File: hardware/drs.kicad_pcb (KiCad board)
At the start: 4 copper layers, 60 x 40 mm, 100 parts, among them IC1 TPS54202HDDCR, J1 USB-C_GCT_USB4145-03-0070-C, J2 FTSH-107-01-L-D-K, J3 POWER & CAN & SPI2, J4 PWM1, J5 PWM2, Q1 SI2347DS-T1-GE3, Q2 LMR51635XDDCR, Q3 LMR51635XDDCR, T1 TP_VCC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

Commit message: signal routing
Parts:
- moved T5 42.5 mm to (207.2, 93.5)
- moved R15 2.00 mm to (162.5, 79.8)
- moved R16 1.55 mm to (162.5, 78.0)
- moved J4 0.60 mm to (174.2, 87.0)
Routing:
- net +3V3: track 3.39 -> 84.5 mm, vias 0 -> 5
- net VCC: track 6.24 -> 79.1 mm, vias 0 -> 7
- net VBUS: track 0.00 -> 49.5 mm, vias 0 -> 6
- net /Connectors/RX: track 0.00 -> 49.2 mm, vias 0 -> 3
- net +6V6S2: track 0.00 -> 48.9 mm, vias 0 -> 2
- net /Connectors/CLK: track 0.00 -> 48.4 mm, vias 0 -> 3
- net /Control/NRST: track 2.96 -> 50.5 mm, vias 0 -> 2
- net +6V6S1: track 0.00 -> 47.5 mm
- net /Connectors/PWM2: track 0.00 -> 43.2 mm, vias 0 -> 2
- net /Connectors/PWM1: track 0.00 -> 43.0 mm, vias 0 -> 1
- net /Connectors/TX: track 0.00 -> 37.3 mm, vias 0 -> 1
- net /Connectors/DIO: track 0.00 -> 36.6 mm, vias 0 -> 1
- net /Connectors/D-: track 0.00 -> 29.4 mm, vias 0 -> 2
- net /Connectors/D+: track 0.00 -> 28.5 mm, vias 0 -> 2
- net CAN_H: track 9.95 -> 38.2 mm, vias 0 -> 1
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- added copper zone on F.Cu, net /Power/+6V6S2_OUT
- added copper zone on B.Cu, net /Power/SW_+6V6S2
- added copper zone on F.Cu, net /Power/SW_+6V6S2

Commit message: usbc changed, foots for electro cap and +5 lay
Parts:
- added C14: 22u, Capacitor_SMD:CP_Elec_4x5.8, F.Cu at (239.6, 99.5)
- added C16: 22u, Capacitor_SMD:CP_Elec_4x5.8, F.Cu at (232.0, 99.5)
- C24, C30, C31: footprint Capacitor_SMD:C_0805_2012Metric -> Capacitor_SMD:C_0805_2012Metric_Pad1.18x1.45mm_HandSolder
- C25: footprint Capacitor_SMD:C_0603_1608Metric -> Capacitor_SMD:C_0603_1608Metric_Pad1.08x0.95mm_HandSolder
- C29: renamed from C28; footprint Capacitor_SMD:C_0805_2012Metric -> Capacitor_SMD:C_0805_2012Metric_Pad1.18x1.45mm_HandSolder
- F4, F5: footprint Fuse:Fuse_1812_4532Metric_Pad1.30x3.40mm_HandSolder -> Fuse:Fuse_0805_2012Metric_Pad1.15x1.40mm_HandSolder
- J1: footprint SamacSys_Parts:USB4145030230C -> Connector_USB:USB_C_Receptacle_GCT_USB4110
- Q3: footprint SamacSys_Parts:SOT95P280X110-6N -> Package_TO_SOT_SMD:SOT-23-6_Handsoldering
- R13: footprint Resistor_SMD:R_0603_1608Metric -> Resistor_SMD:R_0603_1608Metric_Pad0.98x0.95mm_HandSolder
- T11: value TP_+3V3 -> TP_+5V
- T9: value TP_+5V -> TP_+3V3
- moved T4 189.9 mm to (1.02, 1.02)
- moved C14 113.5 mm to (234.2, 88.5)
- moved C15 113.5 mm to (241.4, 88.0)
- moved C16 113.5 mm to (234.2, 93.8)
- moved C19 113.5 mm to (239.7, 88.0)
- moved D5 101.3 mm to (226.9, 109.2), turned to 180 degrees
- moved R11 100.5 mm to (228.1, 111.9)
- moved C24 100.4 mm to (230.9, 106.2)
- moved C25 100.4 mm to (230.9, 108.2)
- moved C27 100.4 mm to (233.6, 111.6)
- moved C29 100.4 mm to (236.8, 110.8)
- moved C30 100.4 mm to (236.8, 113.0)
- moved C31 100.4 mm to (236.8, 115.2)
- moved IC1 100.4 mm to (230.9, 111.4)
- moved L3 100.4 mm to (236.3, 106.4)
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- renumbered C18 to C17, C19 to C18, C17 to C19, C29 to C28
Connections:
- F2 pad 1: +6V6S1 -> /Power/+6V6S1_OUT
- F2 pad 2: /Power/+6V6S1_OUT -> +6V6S1
- T10 pad 1: GND -> /Power/+5V_OUT
- T11 pad 1: /Power/VO_+3.3V -> GND
- T9 pad 1: /Power/+5V_OUT -> /Power/VO_+3.3V
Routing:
- net VCC: track 79.1 -> 0.00 mm, vias 7 -> 0
- net +3V3: track 84.5 -> 6.19 mm, vias 5 -> 0
- net /Control/NRST: track 50.5 -> 0.00 mm, vias 2 -> 0
- net VBUS: track 49.5 -> 0.00 mm, vias 6 -> 0
- net /Connectors/RX: track 49.2 -> 0.00 mm, vias 3 -> 0
- net +6V6S2: track 48.9 -> 0.00 mm, vias 2 -> 0
- net /Connectors/CLK: track 48.4 -> 0.00 mm, vias 3 -> 0
- net +6V6S1: track 47.5 -> 0.00 mm
- net /Connectors/PWM2: track 43.2 -> 0.00 mm, vias 2 -> 0
- net /Connectors/PWM1: track 43.0 -> 0.00 mm, vias 1 -> 0
- net /Connectors/TX: track 37.3 -> 0.00 mm, vias 1 -> 0
- net /Connectors/DIO: track 36.6 -> 0.00 mm, vias 1 -> 0
- net /Connectors/D-: track 29.4 -> 0.00 mm, vias 2 -> 0
- net /Connectors/D+: track 28.5 -> 0.00 mm, vias 2 -> 0
- net CAN_H: track 38.2 -> 9.95 mm, vias 1 -> 0
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- added copper zone on F.Cu, net /Power/+5V_OUT
- added copper zone on F.Cu, net /Power/FB_+5V
- added copper zone on F.Cu, net /Power/SW_+5V

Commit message: pcb & footprint update
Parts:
- removed the C14 at (239.6, 99.5)
- removed the C16 at (232.0, 99.5)
- C14, C16: footprint SamacSys_Parts:CAPPM7343X310N -> Capacitor_SMD:CP_Elec_4x5.8
- C20, C21, C22, C23: footprint Capacitor_SMD:C_0603_1608Metric_Pad1.08x0.95mm_HandSolder -> Capacitor_SMD:C_0805_2012Metric_Pad1.18x1.45mm_HandSolder
- C3, C5: footprint Capacitor_SMD:C_0603_1608Metric_Pad1.08x0.95mm_HandSolder -> Capacitor_SMD:C_0201_0603Metric_Pad0.64x0.40mm_HandSolder
- D1, D2, D3, D7: footprint LED_SMD:LED_0603_1608Metric -> LED_SMD:LED_0603_1608Metric_Pad1.05x0.95mm_HandSolder
- D4: footprint Diode_SMD:D_SOD-323_HandSoldering -> Diode_SMD:D_SMB_Handsoldering
- D6: footprint Diode_SMD:D_SOD-123 -> Diode_SMD:D_SOD-123F
- D8: footprint Package_TO_SOT_SMD:SOT-23 -> Package_TO_SOT_SMD:SOT-23-3
- F1: footprint Fuse:Fuse_1206_3216Metric_Pad1.42x1.75mm_HandSolder -> Fuse:Fuse_0805_2012Metric_Pad1.15x1.40mm_HandSolder
- IC1: footprint Package_TO_SOT_SMD:SOT-23-6 -> Package_TO_SOT_SMD:SOT-23-6_Handsoldering
- J1: value USB-C_GCT_USB4145-03-0070-C -> USB_C_Receptacle_USB2.0_16P; footprint Connector_USB:USB_C_Receptacle_GCT_USB4110 -> Connector_USB:USB_C_Receptacle_GCT_USB4105-xx-A_16P_TopMnt_Horizontal
- Q1: footprint Package_TO_SOT_SMD:SOT-23_Handsoldering -> Package_TO_SOT_SMD:SOT-23-3
- R11, R12: footprint Resistor_SMD:R_0603_1608Metric -> Resistor_SMD:R_0603_1608Metric_Pad0.98x0.95mm_HandSolder
- moved C15 21.8 mm to (220.0, 91.8)
- moved C19 21.8 mm to (218.2, 91.8)
- moved C14 20.7 mm to (218.6, 102.0), turned to 0 degrees
- moved C16 15.2 mm to (219.2, 96.5), turned to 0 degrees
- moved C18 12.8 mm to (233.5, 88.1)
- moved C9 12.8 mm to (240.3, 94.3)
- moved L2 12.8 mm to (236.5, 82.9)
- moved Q3 12.8 mm to (236.2, 90.3)
- moved R10 12.8 mm to (235.3, 94.3)
- moved R9 12.8 mm to (233.5, 92.5)
- moved C11 12.8 mm to (238.7, 94.3)
- moved C13 12.8 mm to (237.1, 94.3)
- moved C21 12.8 mm to (241.8, 80.8)
- moved C23 12.8 mm to (241.8, 79.2)
- moved C7 12.8 mm to (239.1, 89.5)
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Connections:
- D4 pad 2: /Power/RPP_D -> /Power/RPP_G
- D5 pad 2: /Power/RPP_G -> /Power/RPP_S
- F1 pad 2: /Power/RPP_D -> /Power/RPP_G
- J1 pad A6: /Connectors/D- -> /Connectors/D+
- J1 pad B7: /Connectors/D+ -> /Connectors/D-
- J1 pad S1: (no net) -> GND
- Q1 pad 1: /Power/RPP_D -> /Power/RPP_G
- Q1 pad 2: /Power/RPP_G -> /Power/RPP_S
- R6 pad 1: /Power/RPP_G -> /Power/RPP_S
- T3 pad 1: /Power/RPP_D -> /Power/RPP_G
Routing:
- removed copper zone on In2.Cu, net (none)
- removed copper zone on In1.Cu, net GND

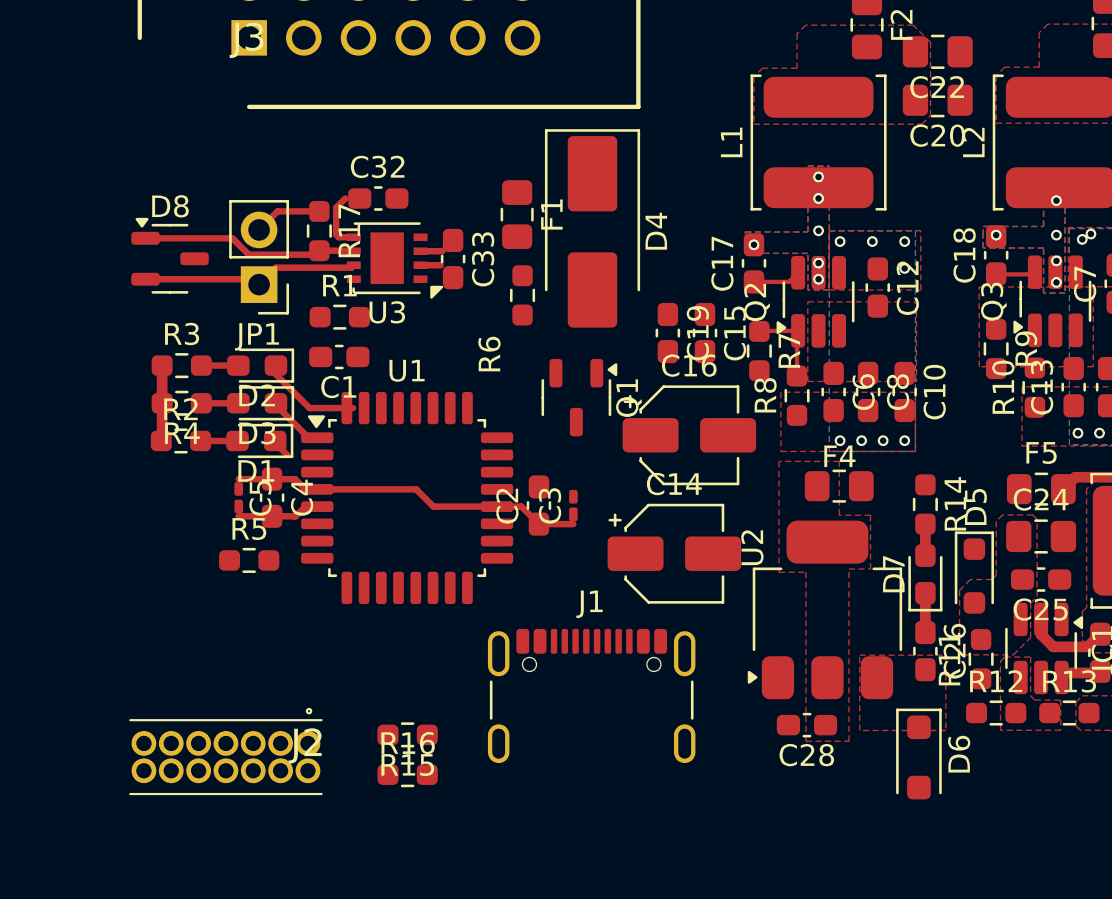
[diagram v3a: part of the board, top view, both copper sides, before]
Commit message: d4 - footprint change
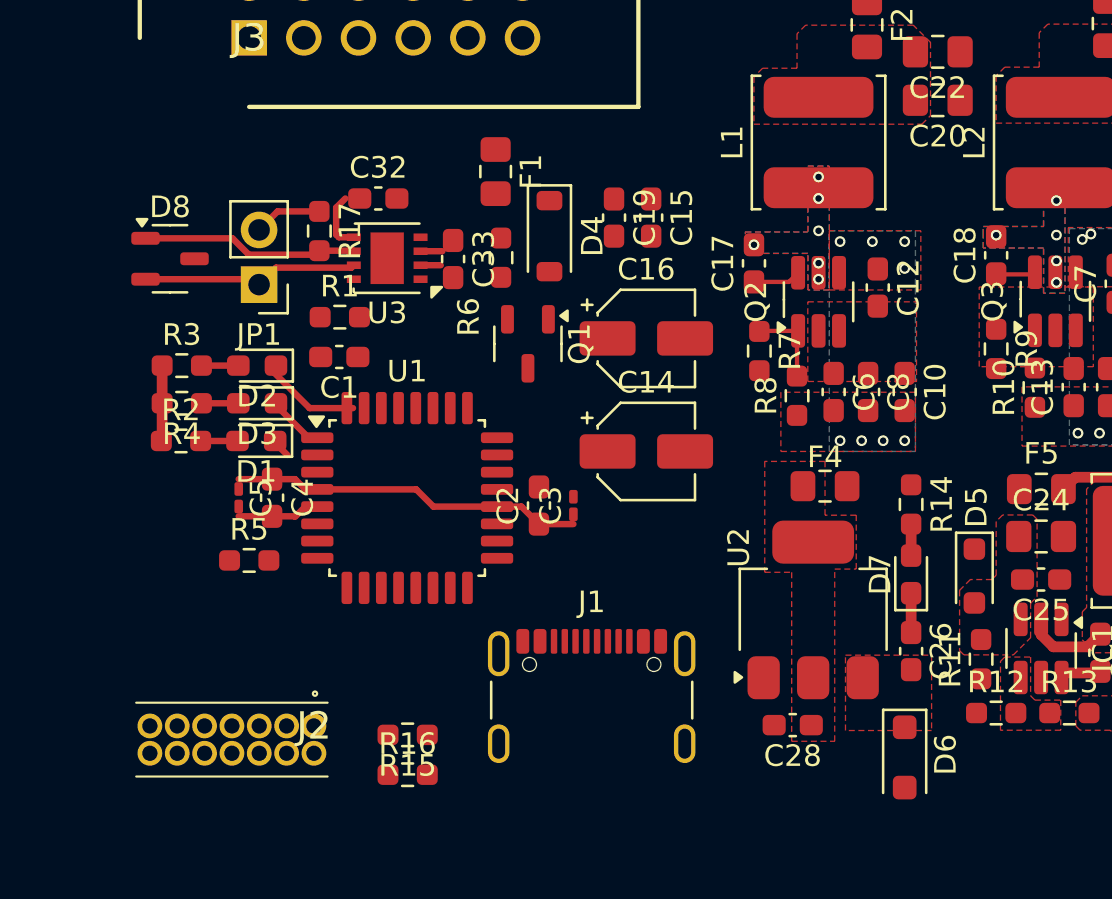
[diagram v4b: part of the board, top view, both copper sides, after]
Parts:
- D4: value 600W/28V -> 200W/28V; footprint Diode_SMD:D_SMB_Handsoldering -> Diode_SMD:D_SOD-123
- moved C15 5.92 mm to (217.5, 86.4)
- moved C19 5.92 mm to (215.8, 86.4)
- moved C14 4.92 mm to (217.2, 97.2)
- moved C16 4.92 mm to (217.2, 92.0)
- moved Q1 3.36 mm to (211.8, 92.2)
- moved F1 2.24 mm to (210.2, 84.2)
- moved R6 2.02 mm to (210.5, 88.2)
- moved D4 2.01 mm to (212.8, 87.2)
- moved J2 0.86 mm to (201.8, 110.0)
- moved C26 0.66 mm to (229.6, 106.5)
- moved C28 0.66 mm to (224.1, 110.0)
- moved D6 0.66 mm to (229.2, 111.5)
- moved D7 0.66 mm to (229.6, 103.0)
- moved F4 0.66 mm to (225.6, 98.9)
- moved R14 0.66 mm to (229.6, 99.7)
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
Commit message: pcb update
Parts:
- moved T4 232.8 mm to (211.0, 101.5)
- moved C3 74.7 mm to (139.2, 102.3)
- moved C1 74.4 mm to (128.6, 95.5)
- moved C5 74.4 mm to (124.0, 102.0)
- moved D1 74.4 mm to (124.8, 99.3)
- moved D2 74.4 mm to (124.8, 95.8)
- moved D3 74.4 mm to (124.8, 97.6)
- moved R2 74.4 mm to (121.3, 99.3)
- moved R3 74.4 mm to (121.3, 95.8)
- moved R4 74.4 mm to (121.3, 97.6)
- moved C2 74.4 mm to (137.9, 102.3)
- moved C4 74.4 mm to (125.5, 102.0)
- moved R1 74.4 mm to (128.7, 93.6)
- moved R5 74.4 mm to (124.5, 104.9)
- moved U1 74.4 mm to (131.8, 102.0)
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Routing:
- net /Control/STM_VCC: track 15.9 -> 14.3 mm
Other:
- board size 60 x 40 mm -> 70 x 45 mm

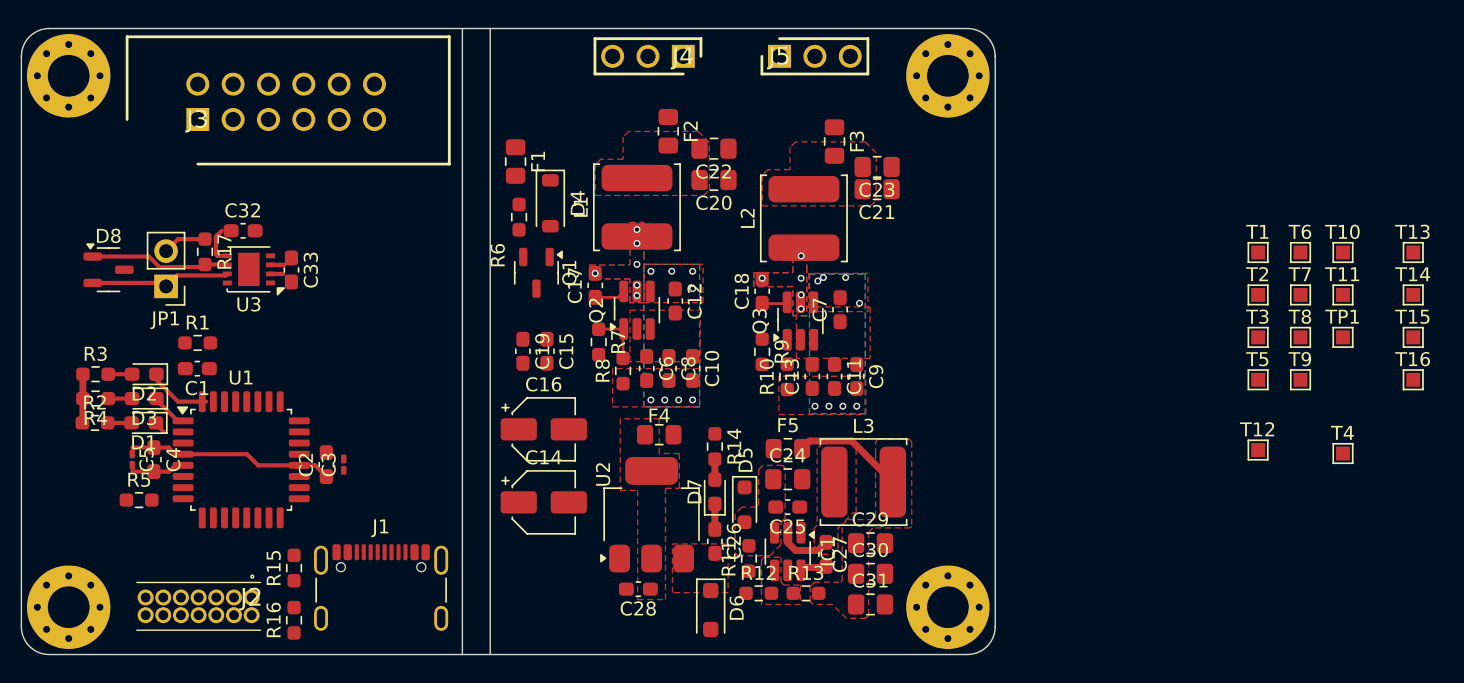
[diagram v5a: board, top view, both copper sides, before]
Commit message: VCC to RPP & RPP to rest routing
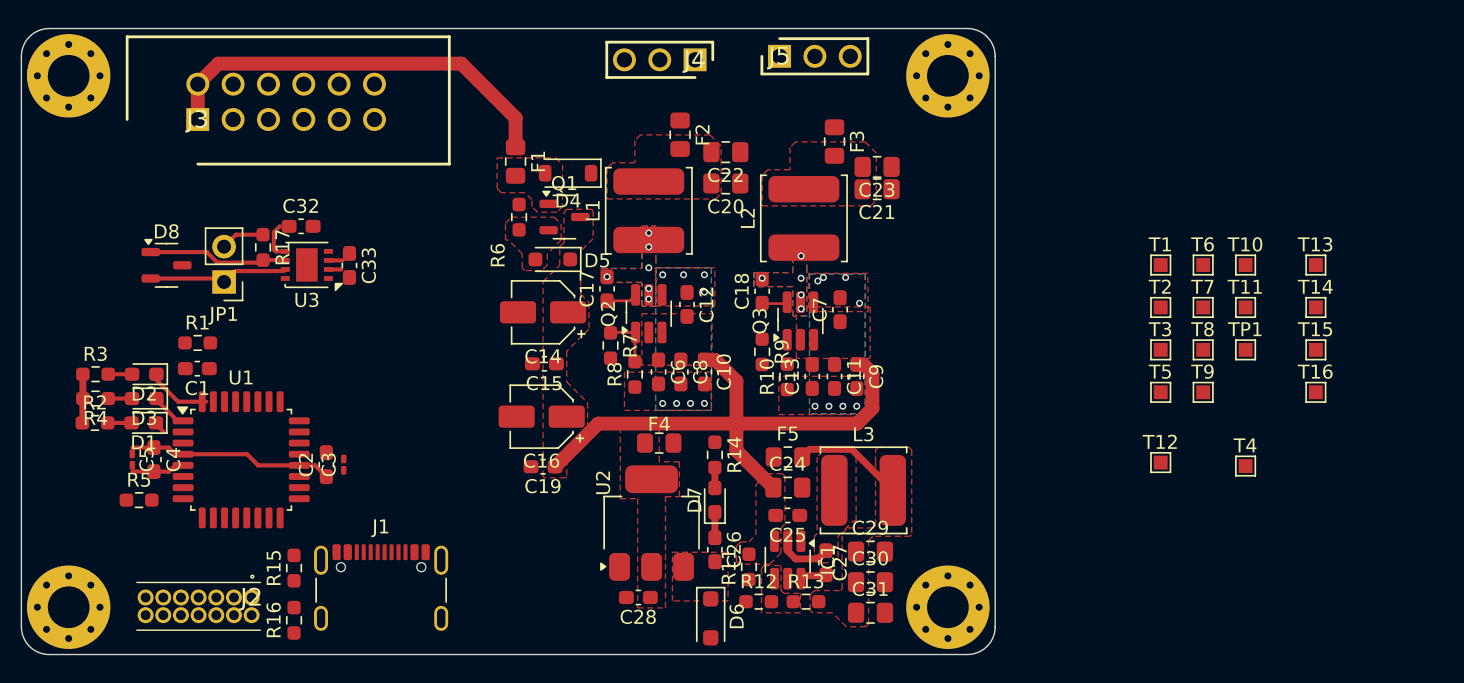
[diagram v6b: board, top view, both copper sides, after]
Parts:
- moved D5 22.4 mm to (154.2, 87.6), turned to 180 degrees
- moved C14 13.7 mm to (153.5, 91.4), turned to 180 degrees
- moved C19 8.43 mm to (153.5, 102.5), turned to 180 degrees
- moved T1 7.06 mm to (197.9, 88.0)
- moved T10 7.06 mm to (204.0, 88.0)
- moved T12 7.06 mm to (197.9, 102.2)
- moved T13 7.06 mm to (209.1, 88.0)
- moved T16 7.06 mm to (209.1, 97.2)
- moved T4 7.06 mm to (204.0, 102.5)
- moved T5 7.06 mm to (197.9, 97.2)
- moved T6 7.06 mm to (200.9, 88.0)
- moved T9 7.06 mm to (200.9, 97.2)
- moved T11 7.06 mm to (204.0, 91.0)
- moved T14 7.06 mm to (209.1, 91.0)
- moved T15 7.06 mm to (209.1, 94.1)
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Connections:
- C10 pad 1: VCC -> /Power/VCC_IN
- C11 pad 1: VCC -> /Power/VCC_IN
- C12 pad 2: VCC -> /Power/VCC_IN
- C13 pad 2: VCC -> /Power/VCC_IN
- C14 pad 1: VCC -> /Power/VCC_IN
- C15 pad 1: VCC -> /Power/VCC_IN
- C16 pad 1: VCC -> /Power/VCC_IN
- C19 pad 1: VCC -> /Power/VCC_IN
- C24 pad 1: VCC -> /Power/VCC_IN
- C25 pad 2: VCC -> /Power/VCC_IN
- C6 pad 1: VCC -> /Power/VCC_IN
- C7 pad 1: VCC -> /Power/VCC_IN
- C8 pad 1: VCC -> /Power/VCC_IN
- C9 pad 1: VCC -> /Power/VCC_IN
- D5 pad 1: VCC -> /Power/VCC_IN
- IC1 pad 3: VCC -> /Power/VCC_IN
- Q1 pad 3: VCC -> /Power/VCC_IN
- Q2 pad 2: VCC -> /Power/VCC_IN
- Q2 pad 3: VCC -> /Power/VCC_IN
- Q3 pad 2: VCC -> /Power/VCC_IN
- Q3 pad 3: VCC -> /Power/VCC_IN
- R11 pad 2: VCC -> /Power/VCC_IN
- T1 pad 1: VCC -> /Power/VCC_IN
- T2 pad 1: VCC -> /Power/VCC_IN
- T8 pad 1: VCC -> /Power/VCC_IN
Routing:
- net /Power/VCC_IN: track 0.00 -> 39.8 mm
- net VCC: track 0.00 -> 29.7 mm
- added copper zone on F.Cu, net /Power/RPP_G
- added copper zone on F.Cu, net /Power/RPP_S
- added copper zone on F.Cu, net /Power/VCC_IN
- removed copper zone on F.Cu, net VCC
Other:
- outline, holes or cut-outs redrawn

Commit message: pcb update
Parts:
- moved R14 2.34 mm to (163.6, 101.0), turned to 0 degrees
- moved F4 2.16 mm to (159.7, 101.0), turned to 0 degrees
- moved D6 1.52 mm to (164.5, 112.3), turned to 180 degrees
- moved C3 0.92 mm to (139.2, 103.3)
- moved C2 0.69 mm to (137.9, 103.0)
- moved C33 0.42 mm to (140.0, 88.0)
- moved JP1 0.31 mm to (130.7, 88.9)
- moved R17 0.23 mm to (133.4, 86.5)
- moved C11 0.20 mm to (174.4, 96.2)
- moved C13 0.20 mm to (172.8, 96.2)
- moved C9 0.20 mm to (176.1, 96.2)
- moved R10 0.20 mm to (171.1, 96.2)
- turned F2 to 90 degrees
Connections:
- D8 pad 1: CAN_L -> /CAN/CAN_N
- D8 pad 2: CAN_H -> /CAN/CAN_P
- JP1 pad 1: CAN_H -> /CAN/CAN_P
- R17 pad 2: CAN_L -> /CAN/CAN_N
- T15 pad 1: CAN_H -> /CAN/CAN_P
- T16 pad 1: CAN_L -> /CAN/CAN_N
- U3 pad 6: CAN_L -> /CAN/CAN_N
- U3 pad 7: CAN_H -> /CAN/CAN_P
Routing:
- net GND: track 6.12 -> 27.6 mm, vias 16 -> 57
- net /CAN/RXD: track 0.00 -> 20.1 mm
- net /Connectors/TX: track 0.00 -> 19.0 mm, vias 0 -> 2
- net /Connectors/CLK: track 0.00 -> 18.9 mm, vias 0 -> 2
- net /Connectors/RX: track 0.00 -> 16.2 mm, vias 0 -> 2
- net /Control/NRST: track 0.00 -> 14.9 mm
- net /CAN/TXD: track 0.00 -> 13.8 mm
- net /Connectors/D+: track 0.00 -> 13.4 mm
- net /Connectors/D-: track 0.00 -> 12.7 mm
- net +5V: track 1.01 -> 13.4 mm, vias 0 -> 2
- net /Control/STM_VCC: track 14.3 -> 25.4 mm, vias 0 -> 2
- net /CAN/CAN_N: track 0.00 -> 10.1 mm
- net /CAN/CAN_P: track 0.00 -> 10.1 mm
- net /Connectors/USB_CC2: track 0.00 -> 10.0 mm
- net CAN_H: track 9.95 -> 0.00 mm
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- added copper zone on In1.Cu, net GND
- added copper zone on In2.Cu, net GND
